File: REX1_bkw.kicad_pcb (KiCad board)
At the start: 2 copper layers, 16 x 38.2 mm, 10 parts, among them J1 Molex_DIP28_edge_contacts, J2 JTAG, J3 PRG, U1 XCR3064XL-10VQ44, U2 29F800, U3 LP2980

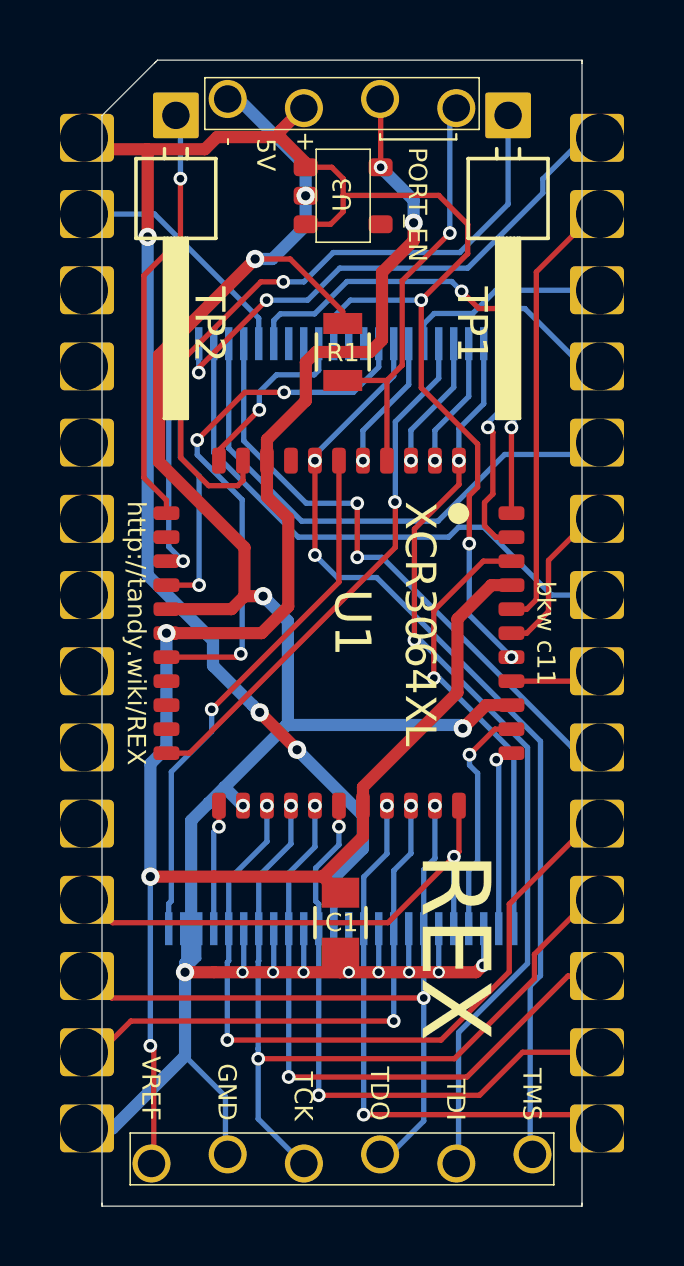
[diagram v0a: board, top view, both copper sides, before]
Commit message: slightly reduced outside dimensions or 3d print variability
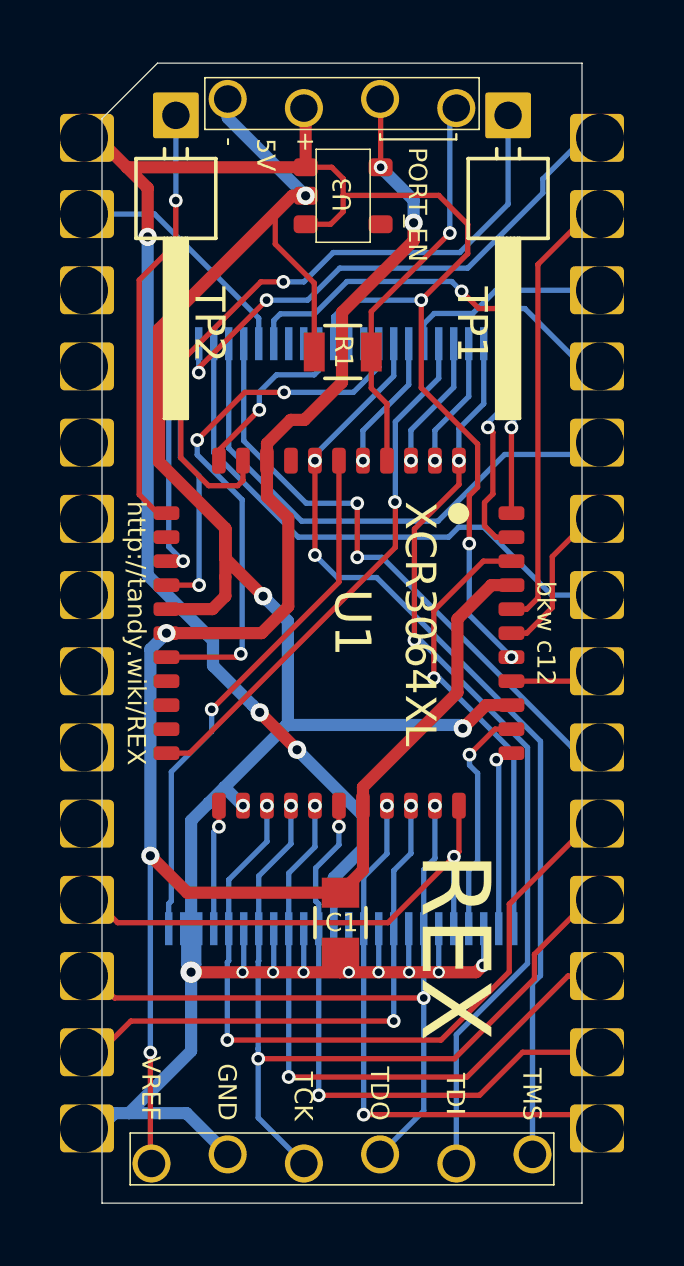
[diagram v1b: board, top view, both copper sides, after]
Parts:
- turned R1 to 180 degrees
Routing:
- net GND: track 88.5 -> 90.2 mm, vias 14 -> 13
- net /PORT_EN: track 14.2 -> 13.2 mm
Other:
- board size 16 x 38.2 mm -> 16 x 38 mm
- board text added: "bkw c12"
- board text removed: "bkw c11"

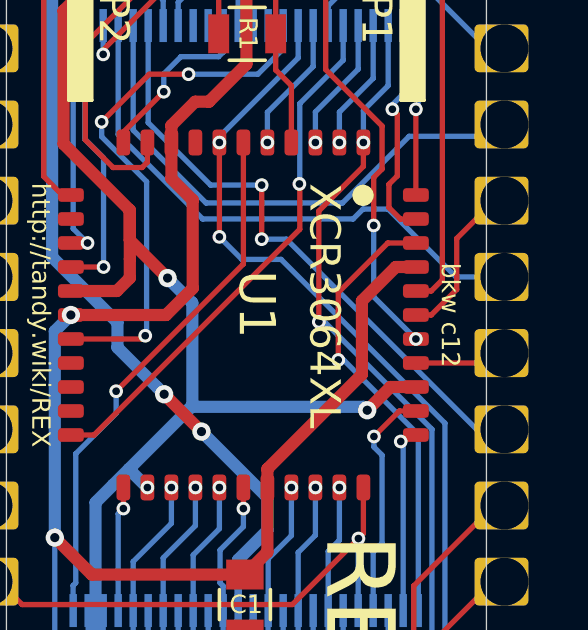
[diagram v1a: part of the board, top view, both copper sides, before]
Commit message: reduce X & Y for 3d printing variability
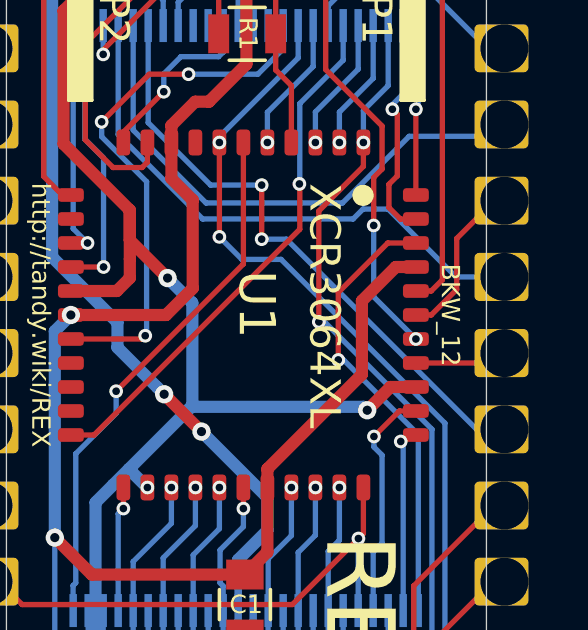
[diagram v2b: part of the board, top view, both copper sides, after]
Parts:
- J1: footprint 000_LOCAL:pcb2molex8878 -> 000_LOCAL:pcb2molex8878_chamfer
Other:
- board text added: "BKW_12"
- board text removed: "bkw c12"
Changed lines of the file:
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@@
   )
   (page A4)
+  (title_block
+    (title REX1_bkw)
+    (rev 12)
+    (comment 1 "Original: Steve Adolph")
+    (comment 2 "Modified: Brian K. White")
+  )
   (layers
     (0 Top signal)
@@
   )
   (setup
-    (last_trace_width 0.4064)
+    (last_trace_width 0.1778)
     (user_trace_width 0.1778)
     (user_trace_width 0.3048)
@@
     (add_net GND)
   )
-  (module 000_LOCAL:pcb2molex8878 locked (layer Top)
+  (module 000_LOCAL:pcb2molex8878_chamfer locked (layer Top)
     (at 147.2184 99.187)
     (descr "Castellated edge contacts to fit Molex 8878 Socket")
@@
     (effects (font (size 0.6096 0.6096) (thickness 0.0762)))
   )
-  (gr_text "bkw c12" (at 154.0129 99.187 -90) (layer F.SilkS)
+  (gr_text BKW_12 (at 154.0129 99.187 -90) (layer F.SilkS)
     (effects (font (size 0.6096 0.6096) (thickness 0.0508)))
   )

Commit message: nonsense trace nudging
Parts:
- moved TP1 0.40 mm to (153.2, 81.9)
- moved TP2 0.40 mm to (141.3, 81.9)
- moved C1 0.18 mm to (147.1, 108.7)
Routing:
- net /+5: track 68.3 -> 69.6 mm, vias 6 -> 4
- net /LVA15: track 9.45 -> 8.45 mm
- net /LVA16: track 8.00 -> 7.28 mm
- net /AD0: track 17.7 -> 17.1 mm
- net /A8: track 7.35 -> 7.94 mm
- net /TP2: track 14.3 -> 14.6 mm, vias 1 -> 0
- net +3V3: track 62.2 -> 62.1 mm, vias 5 -> 4
- net /A10: track 8.11 -> 8.07 mm, vias 0 -> 1
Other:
- net class Default: via_drill 0.3048 -> 0.254
- board text added: "3.3V OUT"
- board text added: "5V IN"
- board text added: "C1: 1uf"
- board text added: "R1: 10k"
- board text added: "U3: LP2980-3.3"
- board text removed: "3.3V out"
- board text removed: "5V in"
- board text removed: "C1=1uf"
- board text removed: "R1=10k"
- board text removed: "U3=LP2980-3.3"

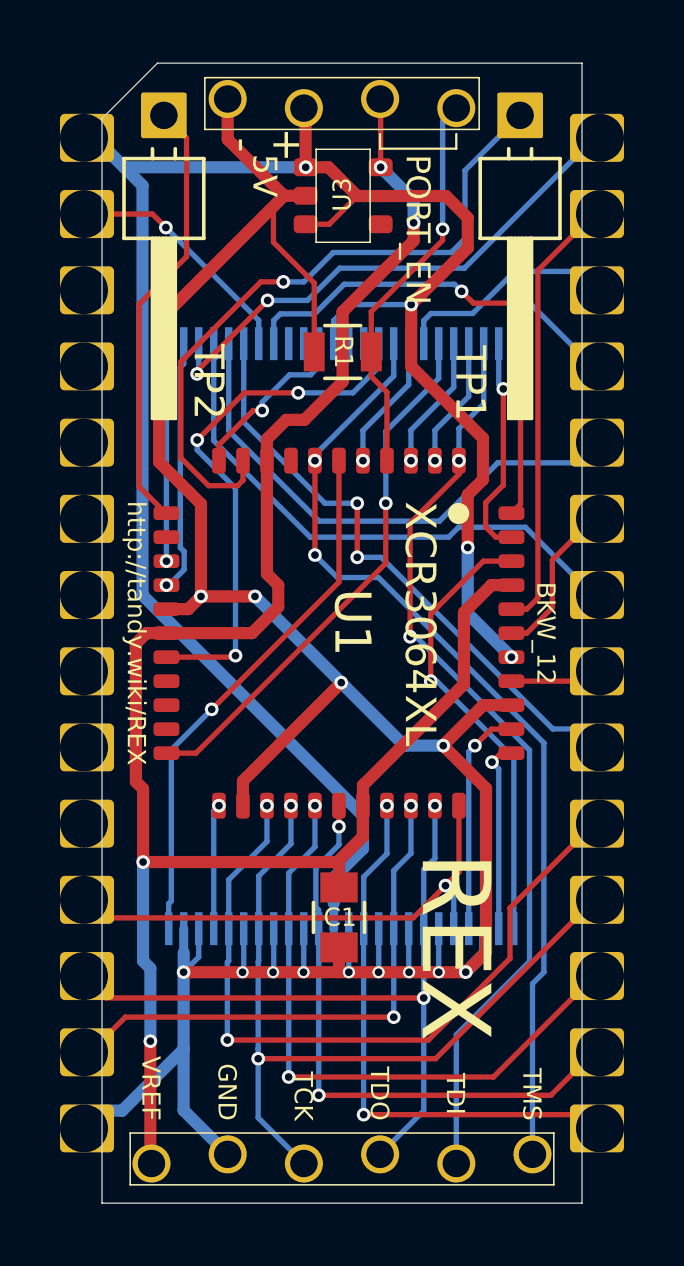
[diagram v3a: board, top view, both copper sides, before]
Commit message: move TP1 & TP2 pins so dupont connector fits better between cpld and socket
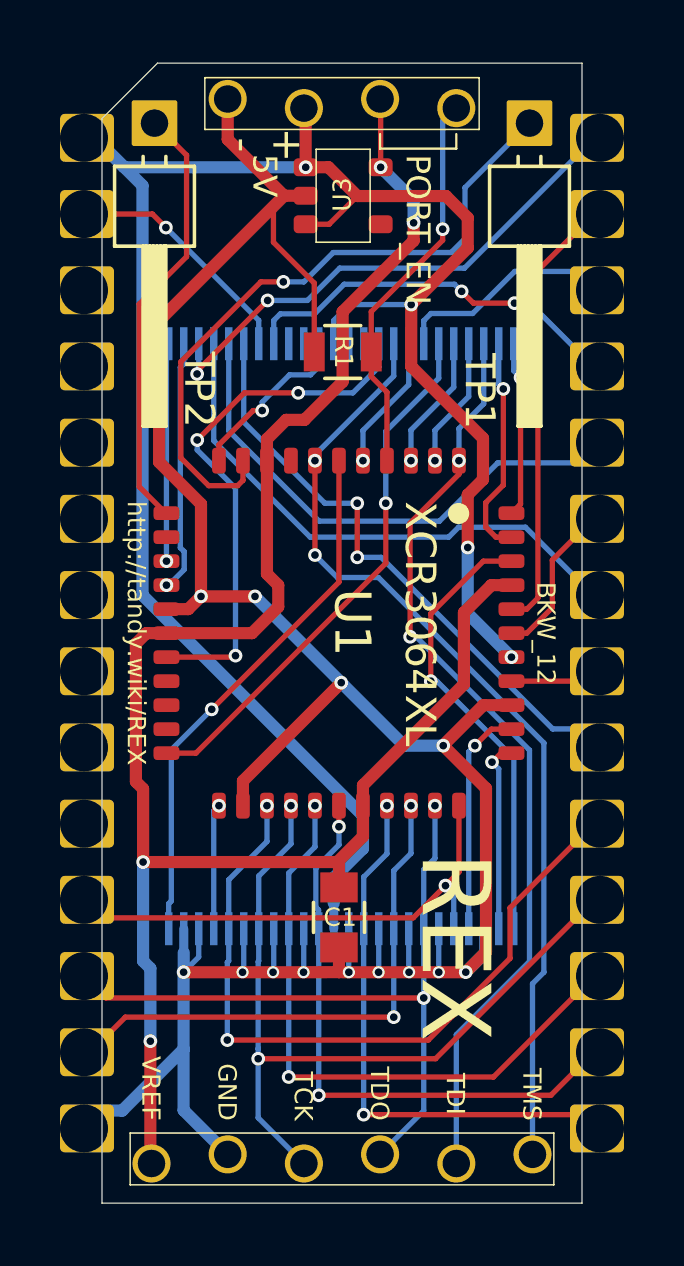
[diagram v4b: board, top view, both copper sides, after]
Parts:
- moved TP1 0.41 mm to (153.5, 82.2)
- moved TP2 0.41 mm to (141.0, 82.2)
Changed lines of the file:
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@@
   )
   (module 000_LOCAL:1x1_pin_h (layer Top)
-    (at 153.1556 81.9277 270)
+    (at 153.4684 82.187 270)
     (descr "Through hole angled pin header, 1x01, 2.54mm pitch, 6mm pin length, single row")
     (tags "Through hole angled pin header THT 1x01 2.54mm single row")
@@
   )
   (module 000_LOCAL:1x1_pin_h (layer Top)
-    (at 141.2812 81.9277 270)
+    (at 140.9684 82.187 270)
     (descr "Through hole angled pin header, 1x01, 2.54mm pitch, 6mm pin length, single row")
     (tags "Through hole angled pin header THT 1x01 2.54mm single row")
@@
   (segment (start 152.8668 99.187) (end 153.3779 99.187) (width 0.1778) (layer Top) (net 33))
   (segment (start 153.3779 99.187) (end 154.2284 98.3365) (width 0.1778) (layer Top) (net 33))
-  (segment (start 142.0384 82.6849) (end 142.0384 86.637) (width 0.1778) (layer Top) (net 34))
+  (segment (start 142.0384 83.257) (end 142.0384 86.637) (width 0.1778) (layer Top) (net 34))
+  (segment (start 141.3384 95.187) (end 141.3668 95.187) (width 0.1778) (layer Top) (net 34))
   (segment (start 140.4584 94.307) (end 141.3384 95.187) (width 0.1778) (layer Top) (net 34))
-  (segment (start 141.2812 81.9277) (end 142.0384 82.6849) (width 0.1778) (layer Top) (net 34))
+  (segment (start 140.9684 82.187) (end 142.0384 83.257) (width 0.1778) (layer Top) (net 34))
   (segment (start 142.0384 86.637) (end 140.4584 88.217) (width 0.1778) (layer Top) (net 34))
-  (segment (start 141.3384 95.187) (end 141.3668 95.187) (width 0.1778) (layer Top) (net 34))
   (segment (start 140.4584 88.217) (end 140.4584 94.307) (width 0.1778) (layer Top) (net 34))
   (via (at 145.2626 87.4776) (size 0.4572) (drill 0.254) (layers Top Bottom) (net 35))
@@
   (segment (start 142.7734 94.2721) (end 143.7386 94.2721) (width 0.1778) (layer Top) (net 35))
   (segment (start 141.8463 93.345) (end 142.7734 94.2721) (width 0.1778) (layer Top) (net 35))
-  (segment (start 151.3184 83.7649) (end 153.1556 81.9277) (width 0.1778) (layer Bottom) (net 35))
+  (segment (start 151.3184 84.337) (end 153.4684 82.187) (width 0.1778) (layer Bottom) (net 35))
   (segment (start 145.9484 87.4776) (end 146.9263 86.4997) (width 0.1778) (layer Bottom) (net 35))
+  (segment (start 145.2626 87.4776) (end 145.9484 87.4776) (width 0.1778) (layer Bottom) (net 35))
+  (segment (start 151.3184 86.03698) (end 151.3184 84.337) (width 0.1778) (layer Bottom) (net 35))
   (segment (start 146.9263 86.4997) (end 150.85568 86.4997) (width 0.1778) (layer Bottom) (net 35))
-  (segment (start 145.2626 87.4776) (end 145.9484 87.4776) (width 0.1778) (layer Bottom) (net 35))
   (segment (start 150.85568 86.4997) (end 151.3184 86.03698) (width 0.1778) (layer Bottom) (net 35))
-  (segment (start 151.3184 86.03698) (end 151.3184 83.7649) (width 0.1778) (layer Bottom) (net 35))
   (segment (start 155.4884 100.787) (end 155.8184 100.457) (width 0.1778) (layer Top) (net 36))
   (segment (start 152.8668 100.787) (end 155.4884 100.787) (width 0.1778) (layer Top) (net 36))
